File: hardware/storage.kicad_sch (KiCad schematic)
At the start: 1 part, among them J7 Micro_SD_Card_Det2

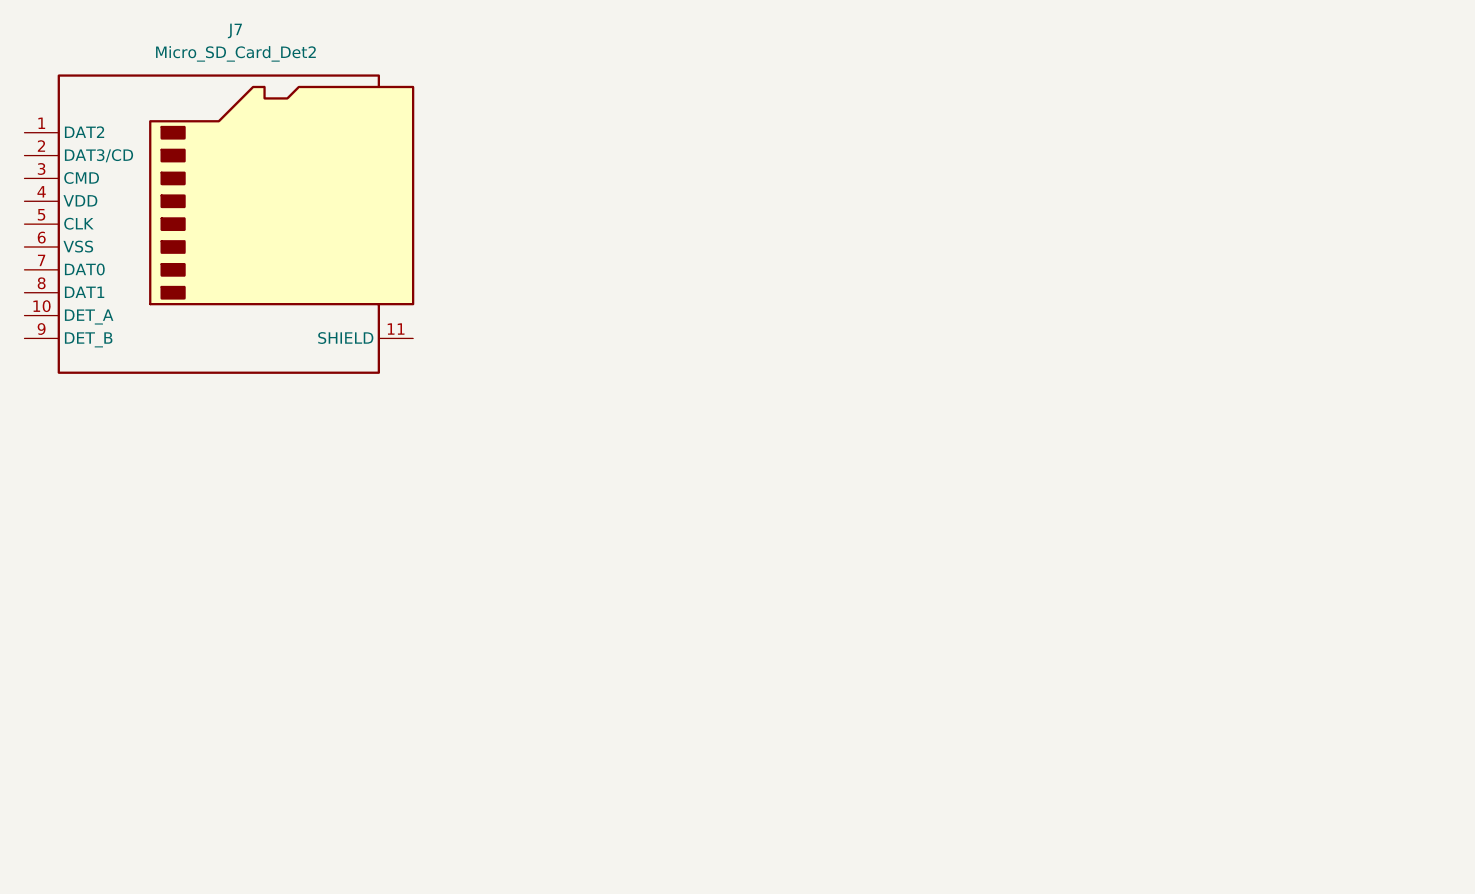
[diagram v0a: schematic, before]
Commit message: Add eMMC and uSD
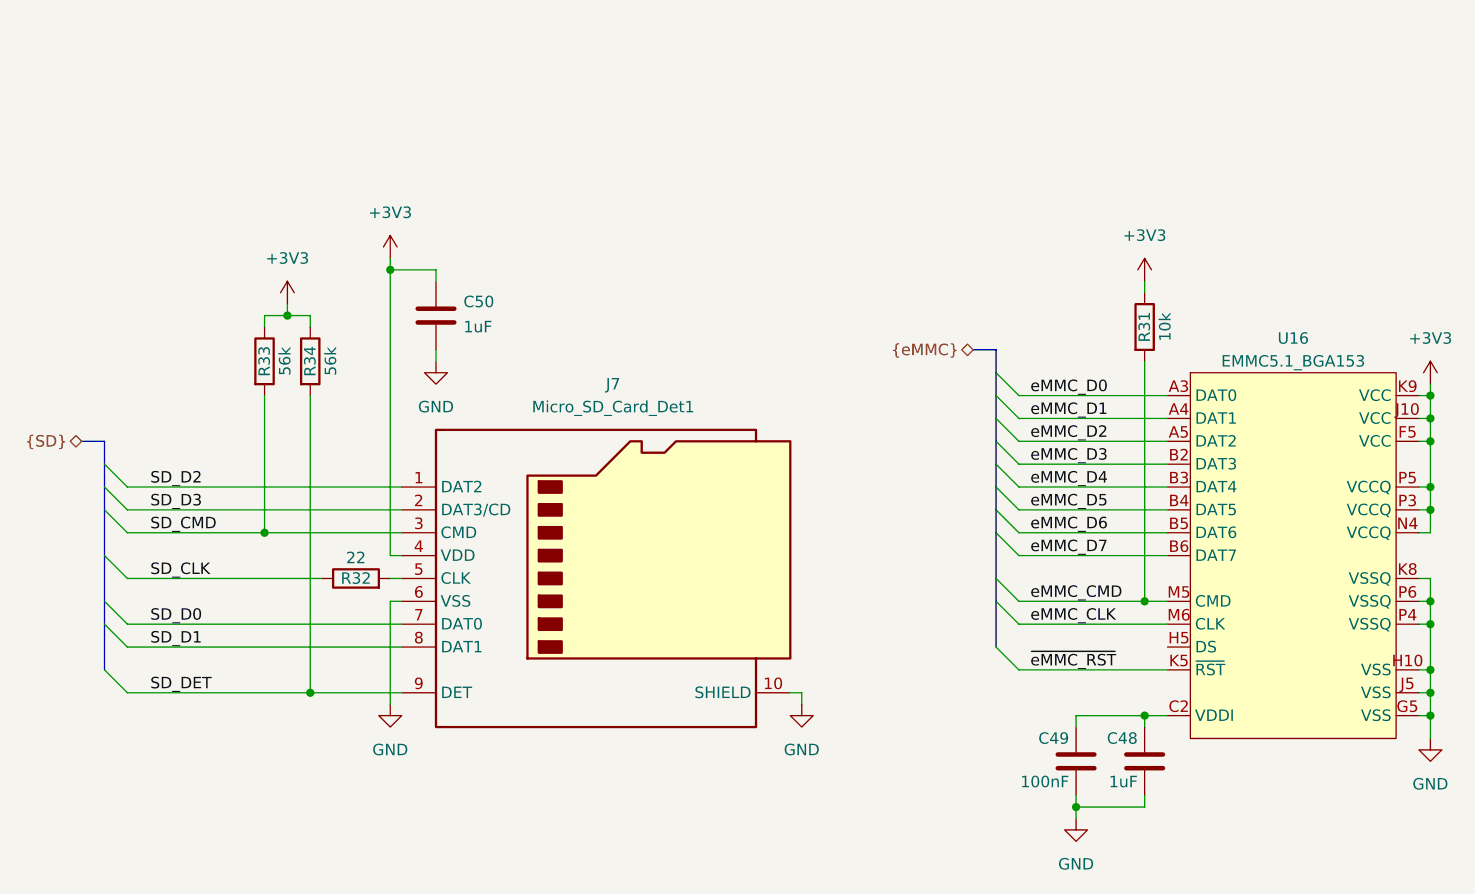
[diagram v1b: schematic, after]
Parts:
- removed J7: Micro_SD_Card_Det2, symbol Connector:Micro_SD_Card_Det2
- added C48, C50: 1uF, Capacitor_SMD:C_0402_1005Metric, symbol Device:C
- added C49: 100nF, Capacitor_SMD:C_0402_1005Metric, symbol Device:C
- added J7: Micro_SD_Card_Det1, cm0:microSD_TF-01A, symbol Connector:Micro_SD_Card_Det1
- added R31: 10k, Resistor_SMD:R_0402_1005Metric, symbol Device:R
- added R32: 22, Resistor_SMD:R_0402_1005Metric, symbol Device:R
- added R33, R34: 56k, Resistor_SMD:R_0402_1005Metric, symbol Device:R
- added U16: EMMC5.1_BGA153, Package_BGA:LFBGA-153_11.5x13mm_Layout14x14_P0.5mm, symbol cm0:EMMC5.1_BGA153
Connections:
- new net: C48.2, C49.1, U16.C2 (VDDI)
- new net: J7.5 (CLK), R32.2
- new net: U16.A1 (NC), U16.A10 (NC), U16.A11 (NC), U16.A12 (NC), U16.A13 (NC), U16.A14 (NC), U16.A2 (NC), U16.A7 (NC), U16.A8 (NC), U16.A9 (NC), U16.B1 (NC), U16.B10 (NC), U16.B11 (NC), U16.B12 (NC), U16.B13 (NC), U16.B14 (NC), U16.B7 (NC), U16.B8 (NC), U16.B9 (NC), U16.C1 (NC), U16.C10 (NC), U16.C11 (NC), U16.C12 (NC), U16.C13 (NC), U16.C14 (NC), U16.C3 (NC), U16.C5 (NC), U16.C7 (NC), U16.C8 (NC), U16.C9 (NC), U16.D1 (NC), U16.D12 (NC), U16.D13 (NC), U16.D14 (NC), U16.D2 (NC), U16.D3 (NC), U16.D4 (NC), U16.E1 (NC), U16.E10 (NC), U16.E12 (NC), U16.E13 (NC), U16.E14 (NC), U16.E2 (NC), U16.E3 (NC), U16.E5 (NC), U16.E8 (NC), U16.E9 (NC), U16.F1 (NC), U16.F10 (NC), U16.F12 (NC), U16.F13 (NC), U16.F14 (NC), U16.F2 (NC), U16.F3 (NC), U16.G1 (NC), U16.G10 (NC), U16.G12 (NC), U16.G13 (NC), U16.G14 (NC), U16.G2 (NC), U16.G3 (NC), U16.H1 (NC), U16.H12 (NC), U16.H13 (NC), U16.H14 (NC), U16.H2 (NC), U16.H3 (NC), U16.J1 (NC), U16.J12 (NC), U16.J13 (NC), U16.J14 (NC), U16.J2 (NC), U16.J3 (NC), U16.K1 (NC), U16.K10 (NC), U16.K12 (NC), U16.K13 (NC), U16.K14 (NC), U16.K2 (NC), U16.K3 (NC), U16.K6 (NC), U16.K7 (NC), U16.L1 (NC), U16.L12 (NC), U16.L13 (NC), U16.L14 (NC), U16.L2 (NC), U16.L3 (NC), U16.M1 (NC), U16.M10 (NC), U16.M11 (NC), U16.M12 (NC), U16.M13 (NC), U16.M14 (NC), U16.M2 (NC), U16.M3 (NC), U16.M7 (NC), U16.M8 (NC), U16.M9 (NC), U16.N1 (NC), U16.N10 (NC), U16.N11 (NC), U16.N12 (NC), U16.N13 (NC), U16.N14 (NC), U16.N3 (NC), U16.N6 (NC), U16.N7 (NC), U16.N8 (NC), U16.N9 (NC), U16.P1 (NC), U16.P10 (NC), U16.P11 (NC), U16.P12 (NC), U16.P13 (NC), U16.P14 (NC), U16.P2 (NC), U16.P7 (NC), U16.P8 (NC), U16.P9 (NC)
- new net +3V3: C50.2, J7.4 (VDD), R31.1, R33.1, R34.1, U16.C6 (VCCQ), U16.E6 (VCC), U16.F5 (VCC), U16.J10 (VCC), U16.K9 (VCC), U16.M4 (VCCQ), U16.N4 (VCCQ), U16.P3 (VCCQ), U16.P5 (VCCQ)
- new net GND: C48.1, C49.2, C50.1, J7.10 (SHIELD), J7.6 (VSS), U16.A6 (VSS), U16.C4 (VSSQ), U16.E7 (VSS), U16.G5 (VSS), U16.H10 (VSS), U16.J5 (VSS), U16.K8 (VSSQ), U16.N2 (VSSQ), U16.N5 (VSSQ), U16.P4 (VSSQ), U16.P6 (VSSQ)
- new net SD_CLK: R32.1
- new net SD_CMD: J7.3 (CMD), R33.2
- new net SD_D0: J7.7 (DAT0)
- new net SD_D1: J7.8 (DAT1)
- new net SD_D2: J7.1 (DAT2)
- new net SD_D3: J7.2 (DAT3/CD)
- new net SD_DET: J7.9 (DET), R34.2
- new net eMMC_CLK: U16.M6 (CLK)
- new net eMMC_CMD: R31.2, U16.M5 (CMD)
- new net eMMC_D0: U16.A3 (DAT0)
- new net eMMC_D1: U16.A4 (DAT1)
- new net eMMC_D2: U16.A5 (DAT2)
- new net eMMC_D3: U16.B2 (DAT3)
- new net eMMC_D4: U16.B3 (DAT4)
- new net eMMC_D5: U16.B4 (DAT5)
- new net eMMC_D6: U16.B5 (DAT6)
- new net eMMC_D7: U16.B6 (DAT7)
- new net ~{eMMC_RST}: U16.K5 (~{RST})
